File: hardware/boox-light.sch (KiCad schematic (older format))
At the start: 24 parts, among them J1 USB_OTG, J2 Passthrough, Q1 BSS138P, U1 MCP73831-2-OT, U2 ATtiny85-20SU

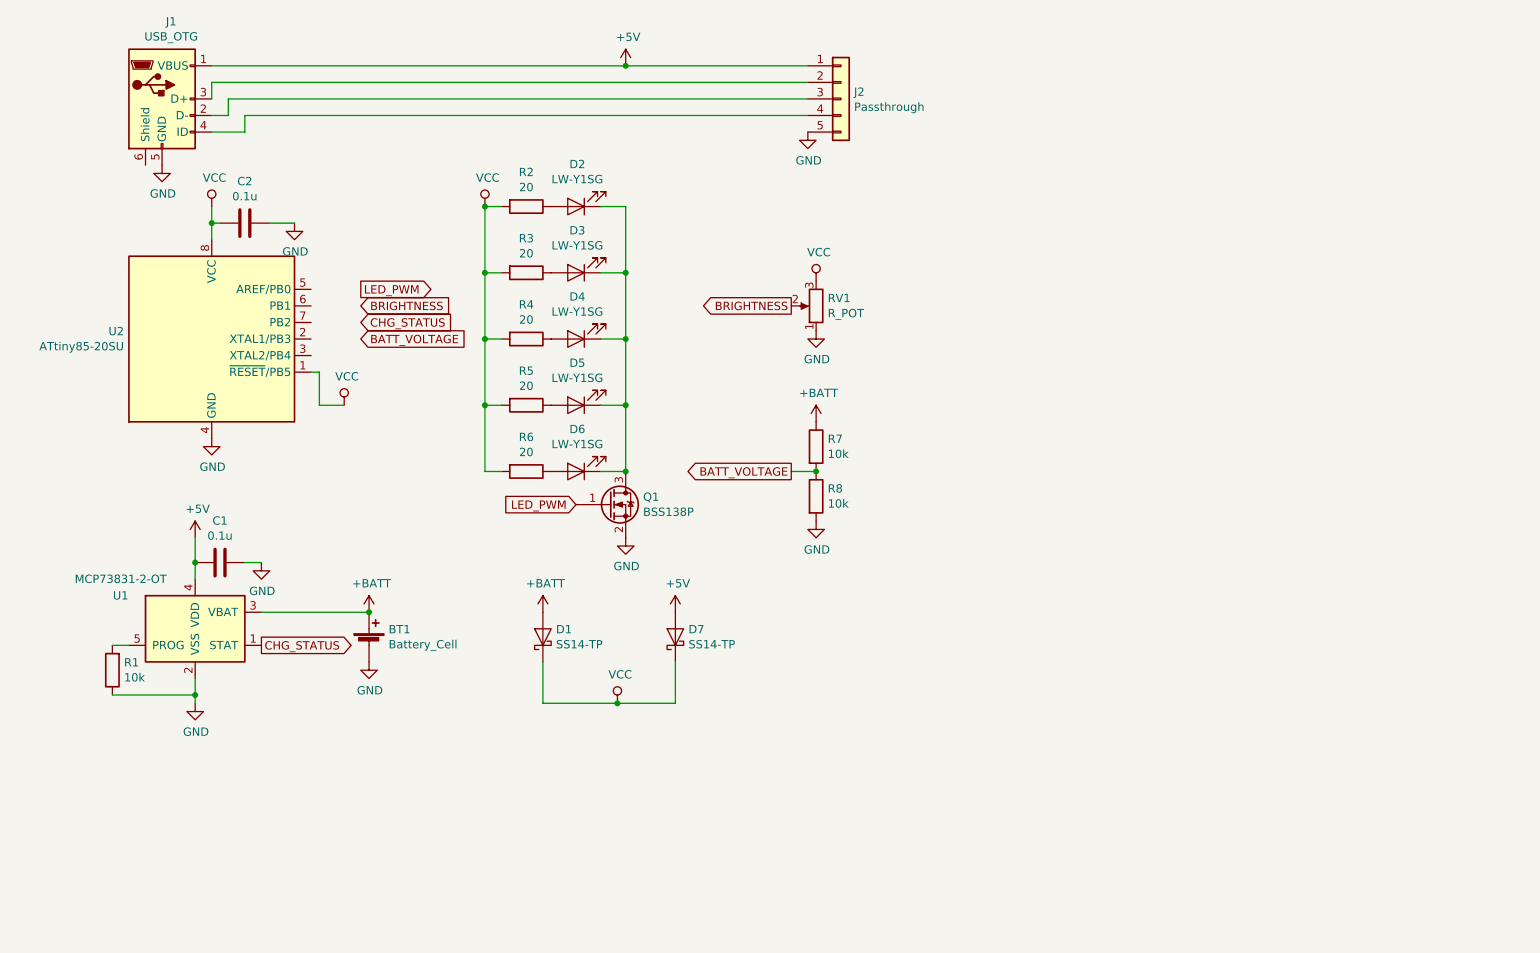
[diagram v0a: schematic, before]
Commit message: Adding completed layout.
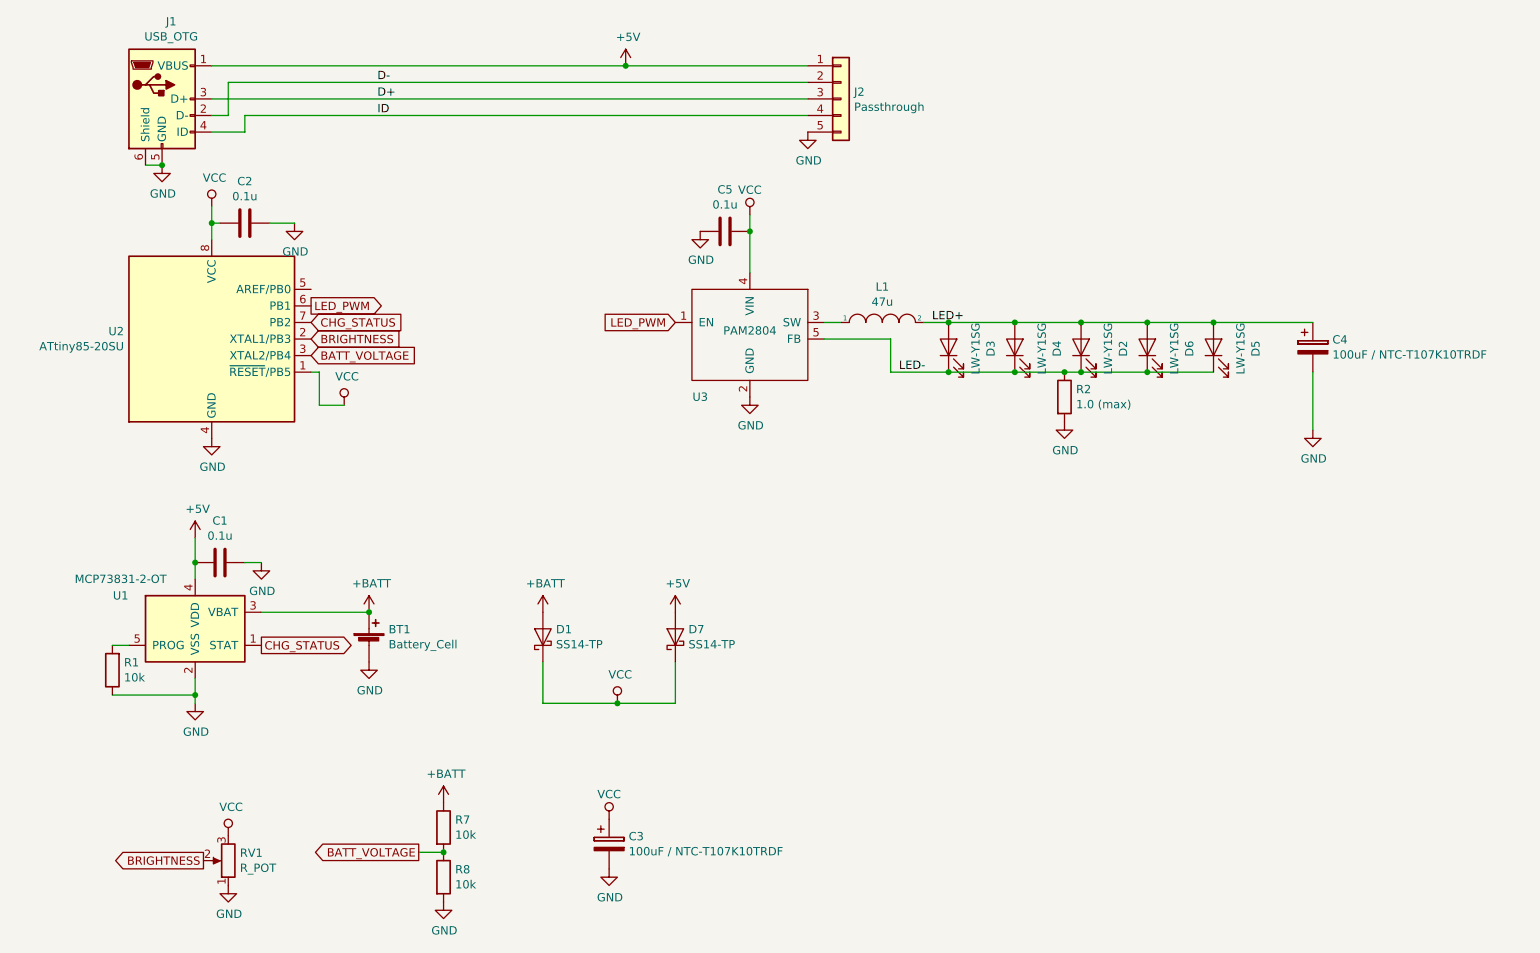
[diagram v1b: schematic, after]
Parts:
- removed Q1: BSS138P, coddingtonbear:SOT-23_LargePads, symbol Device:Q_NMOS_GSD
- removed R3, R4, R5, R6: 20, coddingtonbear:0805_Milling, symbol Device:R
- added C3, C4: 100uF / NTC-T107K10TRDF, coddingtonbear:CP_Tantalum_Case-D_EIA-7343-31_Milling, symbol Device:CP
- added C5: 0.1u, coddingtonbear:0805_Milling, symbol Device:C
- added L1: 47u, Inductor_SMD:L_Bourns-SRN4018, symbol pspice:INDUCTOR
- added U3: PAM2804, Package_TO_SOT_SMD:TSOT-23-5_HandSoldering, symbol coddingtonbear:PAM2804
- R2: value 20 -> 1.0 (max)
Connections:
- net BATT_VOLTAGE: now also U2.3 (XTAL2/PB4)
- net BRIGHTNESS: now also U2.2 (XTAL1/PB3)
- net CHG_STATUS: now also U2.7 (PB2)
- net GND: now also J1.6 (Shield), R2.2, C3.2, C4.2, C5.2, U3.2 (GND)
- net LED_PWM: now also U2.6 (PB1), U3.1 (EN)
- net VCC: now also C3.1, C5.1, U3.4 (VIN); no longer R2.2
- net D+: now reaches J2.3 (Pin_3)
- net D+: now also J1.3 (D+); no longer J1.2 (D-)
- net D-: now reaches J2.2 (Pin_2)
- net D-: now also J1.2 (D-); no longer J1.3 (D+)
- net ID: now reaches J1.4 (ID), J2.4 (Pin_4)
- net LED-: now reaches D2.1 (K), D3.1 (K), D4.1 (K), D5.1 (K), D6.1 (K)
- net LED-: now also R2.1, U3.5 (FB)
- net LED+: now reaches D5.2 (A)
- net LED+: now also D2.2 (A), D3.2 (A), D4.2 (A), D6.2 (A), C4.1, L1.2
- new net: L1.1, U3.3 (SW)
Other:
- moved on the sheet: D2, D3, D4, D5, D6, R7, R8, RV1
